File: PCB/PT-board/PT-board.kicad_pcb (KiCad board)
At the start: 4 copper layers, 22.5 x 23.5 mm, 15 parts, among them J1 Screw_Terminal_01x02, J2 Screw_Terminal_01x02, J3 Conn_01x03_Female, J4 Conn_01x03_Male, U1 MAX31865ATP+

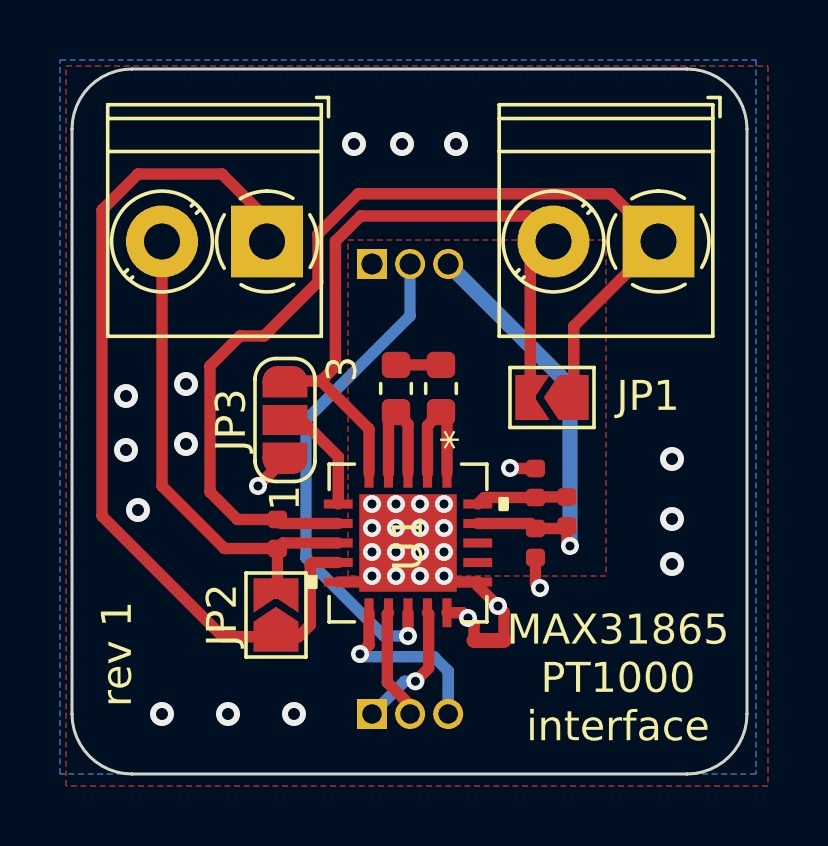
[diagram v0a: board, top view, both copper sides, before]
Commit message: Update PT board size and move filter cap on the Huvud so ethe two boards can actually be attached together.
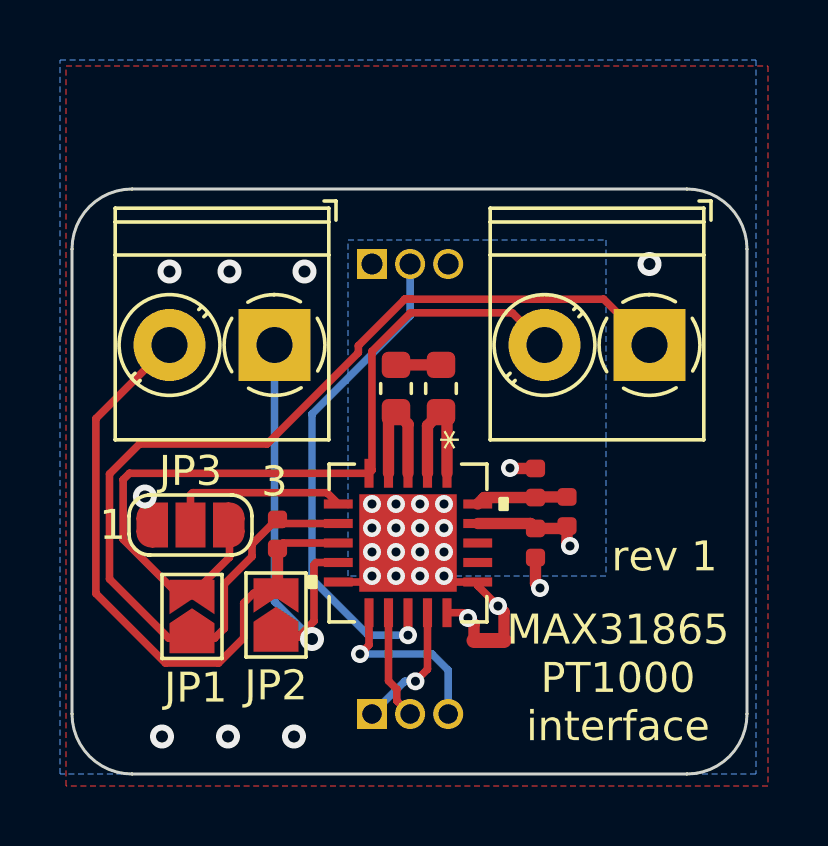
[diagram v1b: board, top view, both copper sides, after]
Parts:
- moved JP1 14.0 mm to (145.0, 122.8), turned to 90 degrees
- moved JP3 4.71 mm to (144.9, 119.7), turned to 0 degrees
- moved J1 3.46 mm to (160.2, 113.7)
- moved J2 3.46 mm to (147.8, 113.7)
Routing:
- net Net-(J2-Pad1): track 29.3 -> 15.8 mm, vias 0 -> 1
- net +3V3: track 14.9 -> 3.78 mm
- net Net-(C1-Pad2): track 16.5 -> 21.5 mm
- net Net-(J1-Pad2): track 23.3 -> 27.0 mm
- net Net-(JP3-Pad2): track 3.86 -> 6.12 mm
- net Net-(C1-Pad1): track 34.2 -> 36.2 mm
- net GNDA: track 6.86 -> 6.62 mm, vias 28 -> 26
- net GND: vias 7 -> 2
- added copper zone on B.Cu, net +3V3
- removed copper zone on F.Cu, net +3V3
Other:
- board size 22.5 x 23.5 mm -> 22.5 x 19.5 mm
